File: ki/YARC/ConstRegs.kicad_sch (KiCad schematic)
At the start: 7 parts, among them U93 74LS32, U94 74HC245, U95 74HC245, U96 74LS32, U97 74HC00, U98 74HC245, U99 74HC245

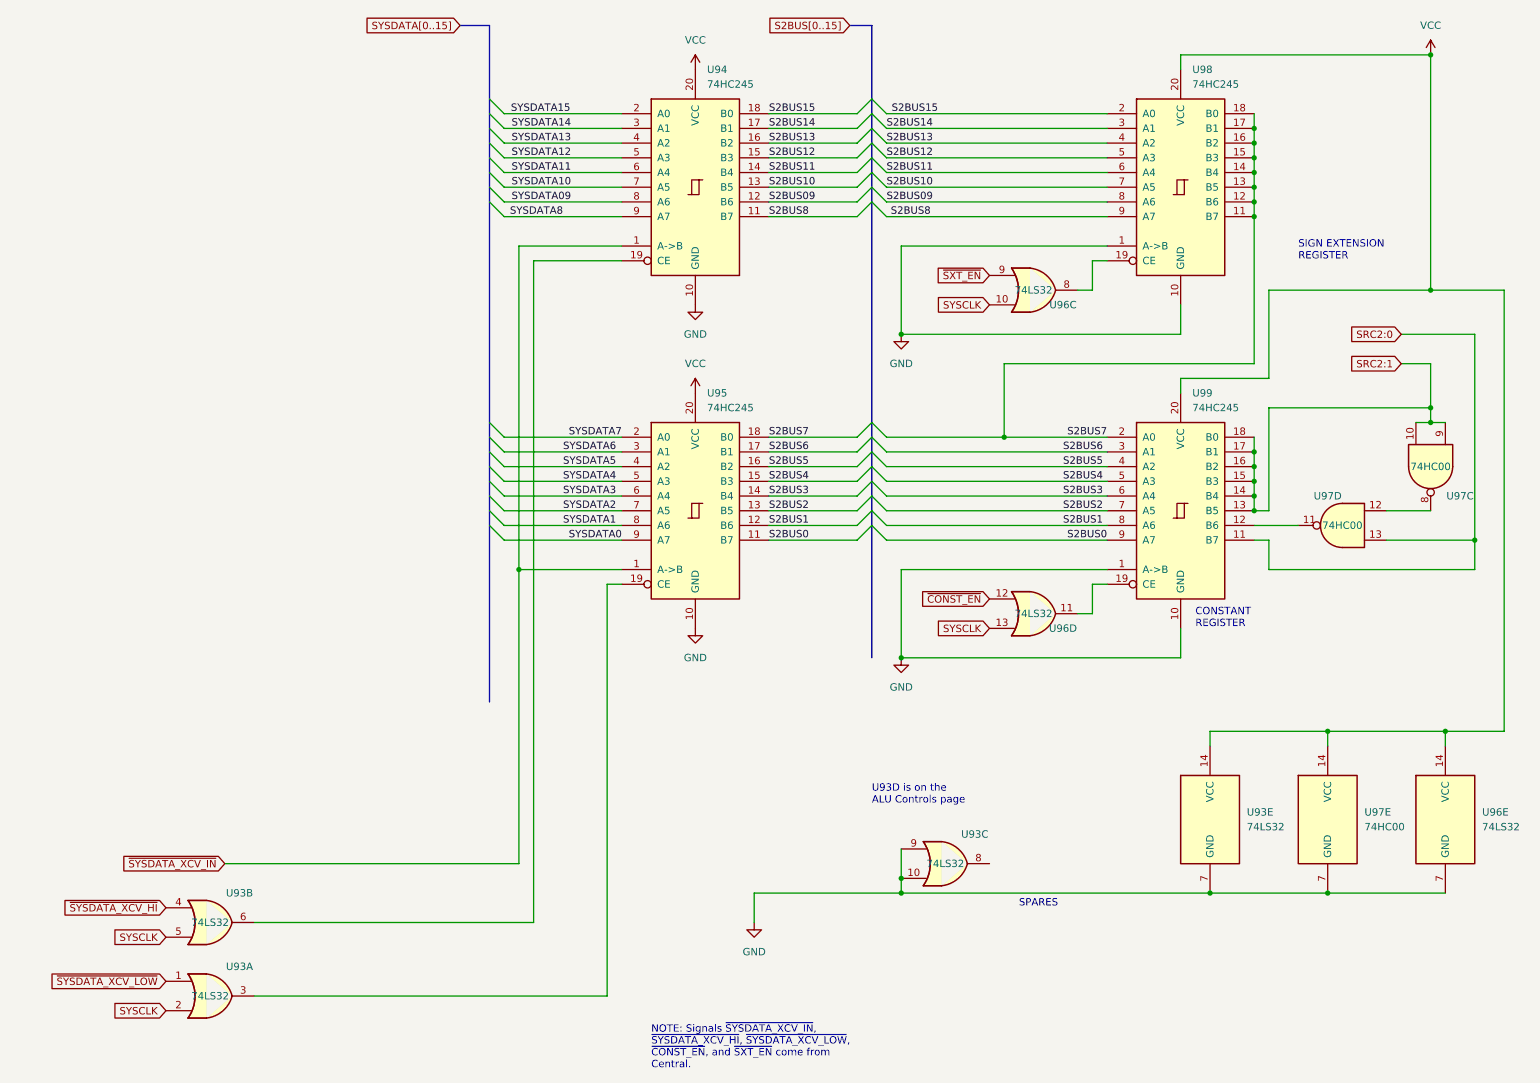
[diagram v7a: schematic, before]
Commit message: Schematic for addressing unit is complete and all ERC violations addressed
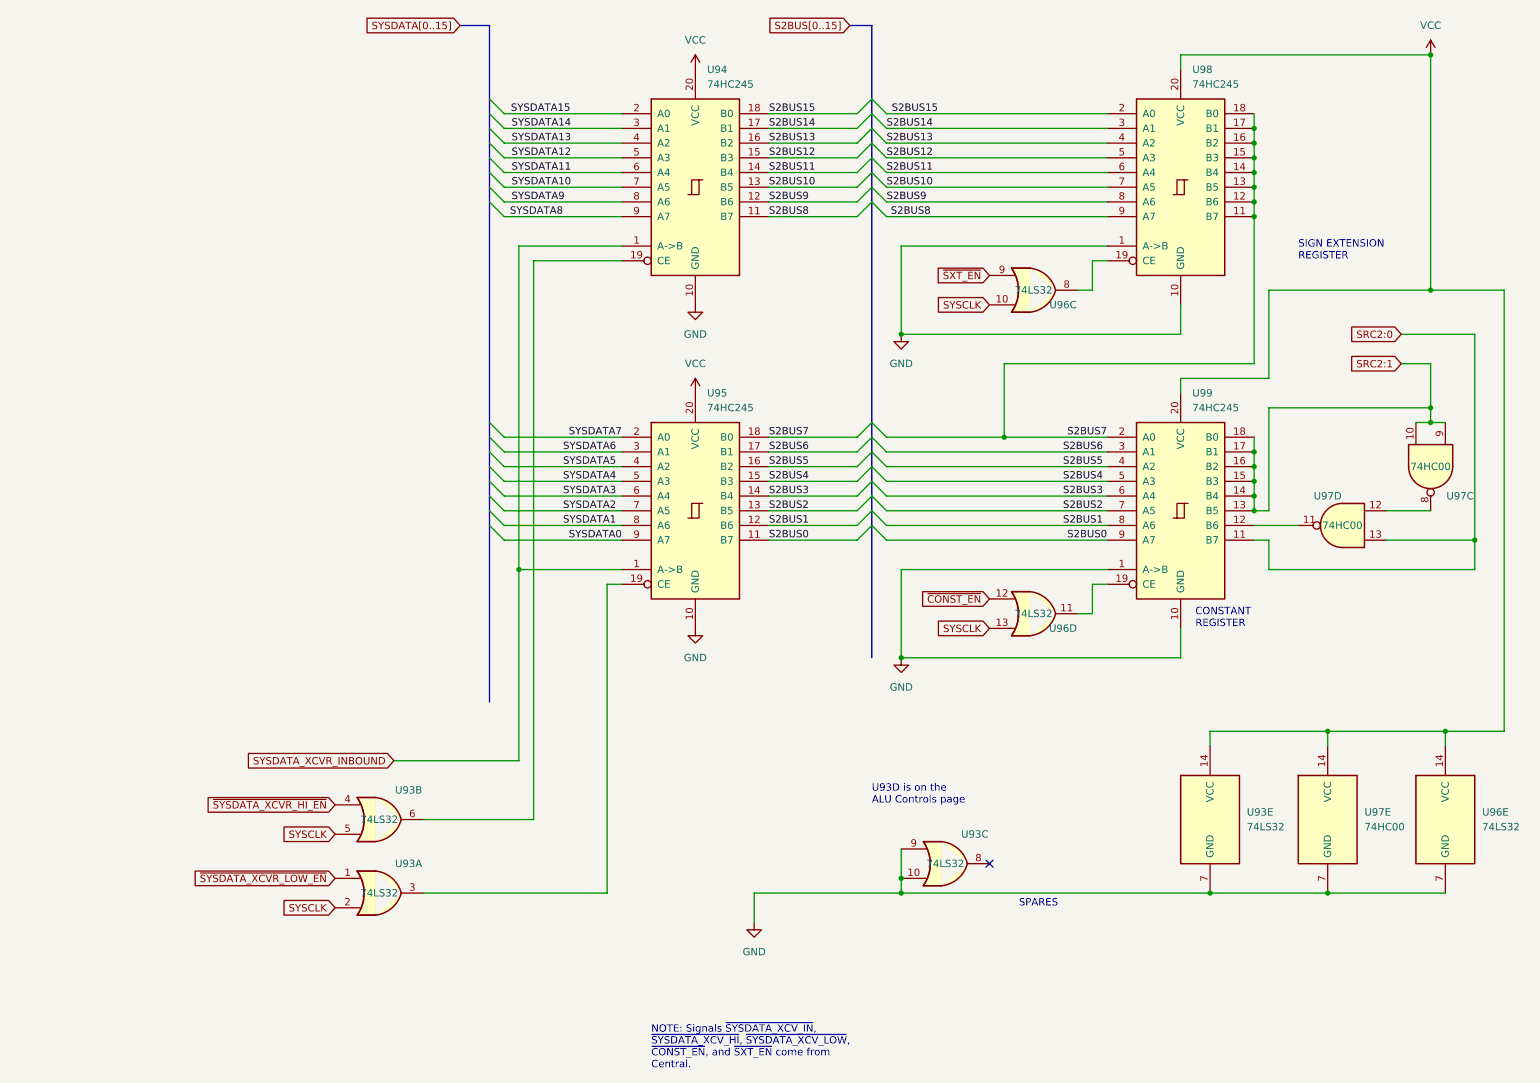
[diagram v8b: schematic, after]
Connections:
- net S2BUS09 renamed S2BUS9
- net SYSDATA09 renamed SYSDATA9
- net ~{SYSDATA_XCV_HI} renamed ~{SYSDATA_XCVR_HI_EN}
- net ~{SYSDATA_XCV_IN} renamed SYSDATA_XCVR_INBOUND
- net ~{SYSDATA_XCV_LOW} renamed ~{SYSDATA_XCVR_LOW_EN}
- no-connect marks 0 -> 1
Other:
- moved on the sheet: U93A, U93B
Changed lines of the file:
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@@
   (junction (at 177.8 88.9) (diameter 0) (color 0 0 0 0)
   )
+  (no_connect (at 175.26 162.56))
   (bus_entry (at 88.9 93.98) (size 2.54 2.54)
     (stroke (width 0) (type default))
@@
     (stroke (width 0) (type default))
   )
-  (wire (pts (xy 96.52 172.72) (xy 96.52 58.42))
+  (wire (pts (xy 96.52 154.94) (xy 96.52 58.42))
     (stroke (width 0) (type default))
   )
@@
     (stroke (width 0) (type default))
   )
-  (wire (pts (xy 109.22 185.42) (xy 109.22 114.3))
+  (wire (pts (xy 109.22 167.64) (xy 109.22 114.3))
     (stroke (width 0) (type default))
   )
@@
     (stroke (width 0) (type default))
   )
+  (bus (pts (xy 154.94 45.72) (xy 154.94 48.26))
+    (stroke (width 0) (type default))
+  )
   (bus (pts (xy 154.94 48.26) (xy 154.94 86.36))
     (stroke (width 0) (type default))
@@
     (stroke (width 0) (type default))
   )
-  (wire (pts (xy 48.26 172.72) (xy 96.52 172.72))
+  (wire (pts (xy 77.47 154.94) (xy 96.52 154.94))
+    (stroke (width 0) (type default))
+  )
+  (bus (pts (xy 154.94 43.18) (xy 154.94 45.72))
     (stroke (width 0) (type default))
   )
@@
     (stroke (width 0) (type default))
   )
-  (bus (pts (xy 154.94 45.72) (xy 154.94 48.26))
-    (stroke (width 0) (type default))
-  )
   (wire (pts (xy 91.44 104.14) (xy 111.76 104.14))
     (stroke (width 0) (type default))
   )
+  (bus (pts (xy 154.94 40.64) (xy 154.94 43.18))
+    (stroke (width 0) (type default))
+  )
   (wire (pts (xy 157.48 48.26) (xy 195.58 48.26))
     (stroke (width 0) (type default))
@@
     (stroke (width 0) (type default))
   )
-  (wire (pts (xy 93.98 162.56) (xy 93.98 111.76))
-    (stroke (width 0) (type default))
-  )
-  (bus (pts (xy 154.94 40.64) (xy 154.94 43.18))
+  (wire (pts (xy 93.98 144.78) (xy 93.98 111.76))
     (stroke (width 0) (type default))
   )
@@
     (stroke (width 0) (type default))
   )
-  (wire (pts (xy 109.22 185.42) (xy 48.26 185.42))
-    (stroke (width 0) (type default))
-  )
-  (bus (pts (xy 154.94 43.18) (xy 154.94 45.72))
+  (wire (pts (xy 109.22 167.64) (xy 77.47 167.64))
     (stroke (width 0) (type default))
   )
@@
     (stroke (width 0) (type default))
   )
-  (wire (pts (xy 43.18 162.56) (xy 93.98 162.56))
+  (wire (pts (xy 72.39 144.78) (xy 93.98 144.78))
     (stroke (width 0) (type default))
   )
@@
     (effects (font (size 1.27 1.27)) (justify left bottom))
   )
-  (label "SYSDATA09" (at 92.71 48.26 0) (fields_autoplaced)
+  (label "SYSDATA9" (at 92.71 48.26 0) (fields_autoplaced)
     (effects (font (size 1.27 1.27)) (justify left bottom))
   )
@@
     (effects (font (size 1.27 1.27)) (justify left bottom))
   )
-  (label "S2BUS09" (at 137.16 48.26 0) (fields_autoplaced)
-    (effects (font (size 1.27 1.27)) (justify left bottom))
-  )
-  (label "S2BUS09" (at 157.48 48.26 0) (fields_autoplaced)
+  (label "S2BUS9" (at 137.16 48.26 0) (fields_autoplaced)
+    (effects (font (size 1.27 1.27)) (justify left bottom))
+  )
+  (label "S2BUS9" (at 157.48 48.26 0) (fields_autoplaced)
     (effects (font (size 1.27 1.27)) (justify left bottom))
   )
@@
   (label "SYSDATA3" (at 101.6 99.06 0) (fields_autoplaced)
     (effects (font (size 1.27 1.27)) (justify left bottom))
+  )
+  (global_label "SYSDATA_XCVR_INBOUND" (shape input) (at 72.39 144.78 180) (fields_autoplaced)
+    (effects (font (size 1.27 1.27)) (justify right))
+    (property "Intersheetrefs" "${INTERSHEET_REFS}" (at 46.2423 144.78 0)
+      (effects (font (size 1.27 1.27)) (justify right) hide)
+    )
   )
   (global_label "SYSDATA[0..15]" (shape input) (at 83.82 17.78 180) (fields_autoplaced)
@@
     )
   )
-  (global_label "SYSCLK" (shape input) (at 33.02 175.26 180) (fields_autoplaced)
+  (global_label "SYSCLK" (shape input) (at 62.23 157.48 180) (fields_autoplaced)
     (effects (font (size 1.27 1.27)) (justify right))
-    (property "Intersheetrefs" "${INTERSHEET_REFS}" (at 23.5312 175.1806 0)
+    (property "Intersheetrefs" "${INTERSHEET_REFS}" (at 52.7412 157.4006 0)
       (effects (font (size 1.27 1.27)) (justify right) hide)
     )
@@
     )
   )
-  (global_label "~{SYSDATA_XCV_HI}" (shape input) (at 33.02 170.18 180) (fields_autoplaced)
+  (global_label "~{SYSDATA_XCVR_LOW_EN}" (shape input) (at 62.23 165.1 180) (fields_autoplaced)
     (effects (font (size 1.27 1.27)) (justify right))
-    (property "Intersheetrefs" "${INTERSHEET_REFS}" (at 15.2459 170.1006 0)
+    (property "Intersheetrefs" "${INTERSHEET_REFS}" (at 37.292 165.1 0)
       (effects (font (size 1.27 1.27)) (justify right) hide)
     )
@@
     )
   )
-  (global_label "~{SYSDATA_XCV_LOW}" (shape input) (at 33.02 182.88 180) (fields_autoplaced)
+  (global_label "~{SYSDATA_XCVR_HI_EN}" (shape input) (at 62.23 152.4 180) (fields_autoplaced)
     (effects (font (size 1.27 1.27)) (justify right))
-    (property "Intersheetrefs" "${INTERSHEET_REFS}" (at 13.3712 182.8006 0)
+    (property "Intersheetrefs" "${INTERSHEET_REFS}" (at 39.1667 152.4 0)
       (effects (font (size 1.27 1.27)) (justify right) hide)
     )
   )
-  (global_label "~{SYSDATA_XCV_IN}" (shape input) (at 43.18 162.56 180) (fields_autoplaced)
+  (global_label "SYSCLK" (shape input) (at 62.23 170.18 180) (fields_autoplaced)
     (effects (font (size 1.27 1.27)) (justify right))
-    (property "Intersheetrefs" "${INTERSHEET_REFS}" (at 25.4059 162.4806 0)
-      (effects (font (size 1.27 1.27)) (justify right) hide)
-    )
-  )
-  (global_label "SYSCLK" (shape input) (at 33.02 187.96 180) (fields_autoplaced)
-    (effects (font (size 1.27 1.27)) (justify right))
-    (property "Intersheetrefs" "${INTERSHEET_REFS}" (at 23.5312 187.8806 0)
+    (property "Intersheetrefs" "${INTERSHEET_REFS}" (at 52.7412 170.1006 0)
       (effects (font (size 1.27 1.27)) (justify right) hide)
     )
@@
     )
   )
-  (symbol (lib_id "74xx:74LS32") (at 40.64 172.72 0) (unit 2)
+  (symbol (lib_id "74xx:74LS32") (at 69.85 154.94 0) (unit 2)
     (in_bom yes) (on_board yes) (dnp no)
-    (property "Reference" "U93" (at 45.72 167.64 0)
-      (effects (font (size 1.27 1.27)))
-    )
-    (property "Value" "74LS32" (at 40.64 172.72 0)
-      (effects (font (size 1.27 1.27)))
-    )
-    (property "Footprint" "" (at 40.64 172.72 0)
-      (effects (font (size 1.27 1.27)) hide)
-    )
-    (property "Datasheet" "http://www.ti.com/lit/gpn/sn74LS32" (at 40.64 172.72 0)
+    (property "Reference" "U93" (at 74.93 149.86 0)
+      (effects (font (size 1.27 1.27)))
+    )
+    (property "Value" "74LS32" (at 69.85 154.94 0)
+      (effects (font (size 1.27 1.27)))
+    )
+    (property "Footprint" "" (at 69.85 154.94 0)
+      (effects (font (size 1.27 1.27)) hide)
+    )
+    (property "Datasheet" "http://www.ti.com/lit/gpn/sn74LS32" (at 69.85 154.94 0)
       (effects (font (size 1.27 1.27)) hide)
     )
@@
     )
   )
-  (symbol (lib_id "74xx:74LS32") (at 40.64 185.42 0) (unit 1)
+  (symbol (lib_id "74xx:74LS32") (at 69.85 167.64 0) (unit 1)
     (in_bom yes) (on_board yes) (dnp no)
-    (property "Reference" "U93" (at 45.72 180.34 0)
-      (effects (font (size 1.27 1.27)))
-    )
-    (property "Value" "74LS32" (at 40.64 185.42 0)
-      (effects (font (size 1.27 1.27)))
-    )
-    (property "Footprint" "" (at 40.64 185.42 0)
-      (effects (font (size 1.27 1.27)) hide)
-    )
-    (property "Datasheet" "http://www.ti.com/lit/gpn/sn74LS32" (at 40.64 185.42 0)
-      (effects (font (size 1.27 1.27)) hide)
-    )
+    (property "Reference" "U93" (at 74.93 162.56 0)
+      (effects (font (size 1.27 1.27)))
+    )
+    (property "Value" "74LS32" (at 69.85 167.64 0)
+      (effects (font (size 1.27 1.27)))
+    )
+    (property "Footprint" "" (at 69.85 167.64 0)
+      (effects (font (size 1.27 1.27)) hide)
+    )
+    (property "Datasheet" "http://www.ti.com/lit/gpn/sn74LS32" (at 69.85 167.64 0)
+      (effects (font (size 1.27 1.27)) hide)
+    )
